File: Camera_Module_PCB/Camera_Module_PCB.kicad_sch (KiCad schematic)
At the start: 0 parts

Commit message: Added Multiple Component CAD Models
Added CAD models for the ESP32-S3, a USB C connector, a SD Card Slot, and an FPC Connector
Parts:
- added J1: FFC2A32-24-T, FFC2A32-24-T:GCT_FFC2A32-24-T, symbol 24 Pin FPC Connector:FFC2A32-24-T
- added J2: DM3AT-SF-PEJM5, DM3AT-SF-PEJM5:HRS_DM3AT-SF-PEJM5, symbol DM3AT-SF-PEJM5 SIM Card:DM3AT-SF-PEJM5
- added P1: USB_C_Plug_USB2.0, symbol Connector:USB_C_Plug_USB2.0
- added SW1: SW_Push, symbol Switch:SW_Push
- added U1: ESP32-S3, ESP32-S3:IC_ESP32-S3, symbol ESP32-S3:ESP32-S3
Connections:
- new net: P1.A1 (GND), P1.A12 (GND), P1.B1 (GND), P1.B12 (GND)
- new net: P1.A4 (VBUS), P1.A9 (VBUS), P1.B4 (VBUS), P1.B9 (VBUS)
- new net: J1.S1 (SHIELD), J1.S2 (SHIELD), J1.S3 (SHIELD), J1.S4 (SHIELD)
- new net VDD3P3: U1.2 (VDD3P3), U1.3 (VDD3P3)
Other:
- note added: "Not Sure if this is the type of USB C we want , but it seems like it"

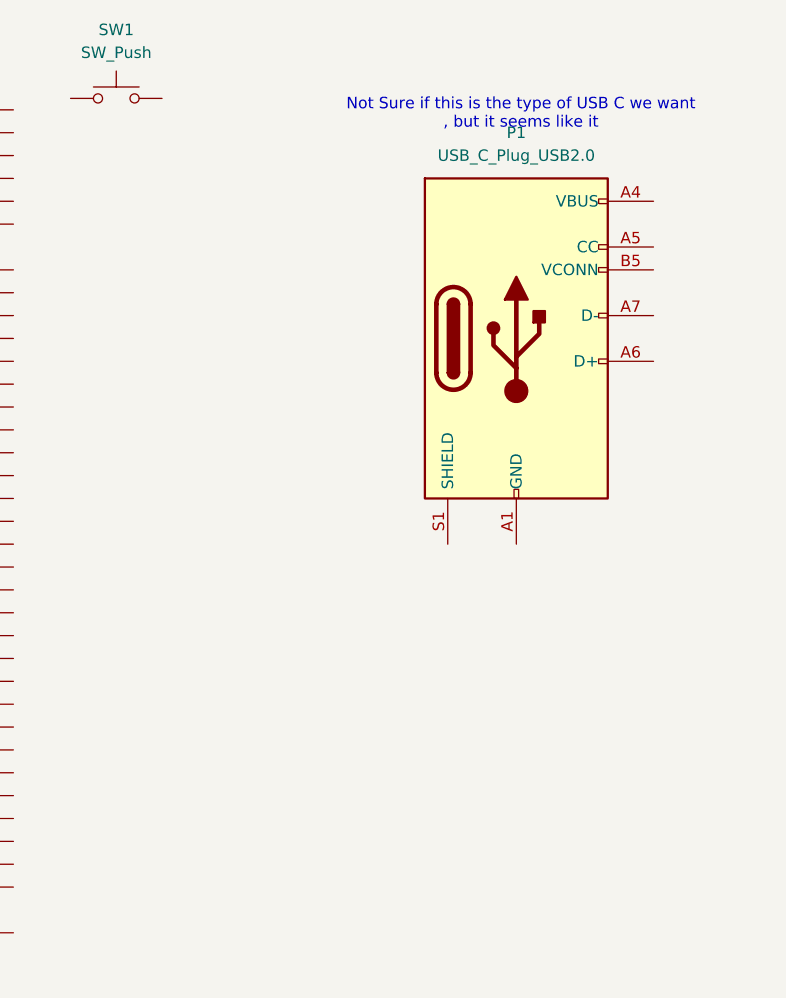
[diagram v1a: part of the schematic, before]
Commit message: Added Extra CAD Models for Voltage
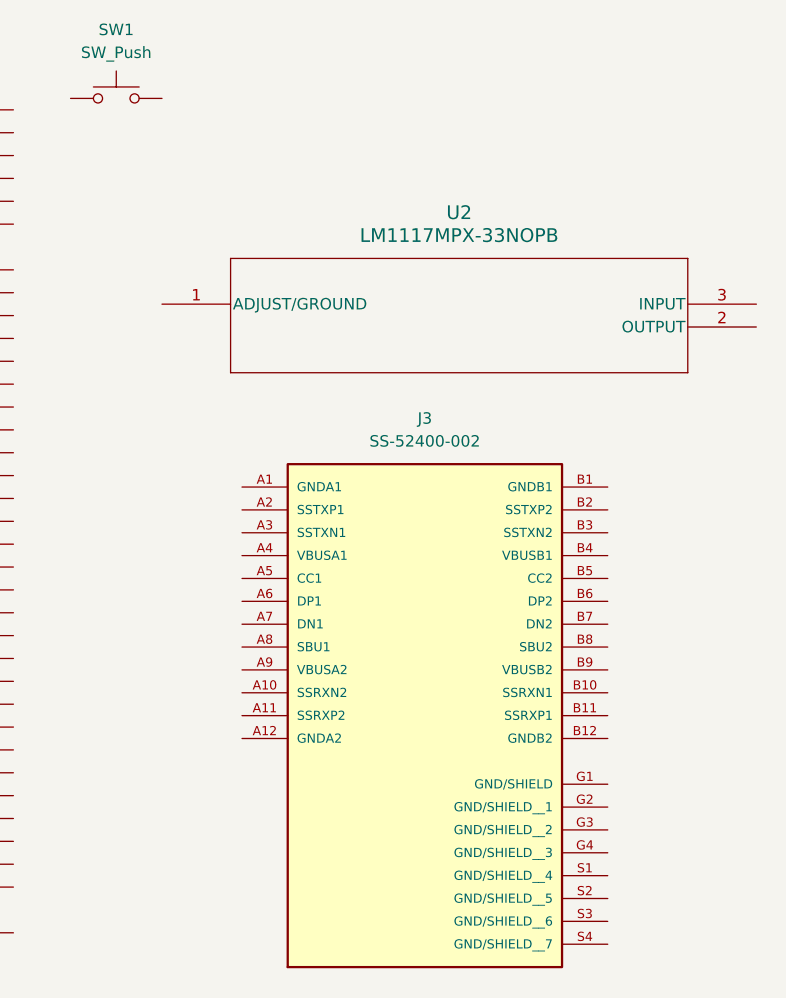
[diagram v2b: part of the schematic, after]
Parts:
- removed P1: USB_C_Plug_USB2.0, symbol Connector:USB_C_Plug_USB2.0
- added J3: SS-52400-002, SS-52400-002:BELFUSE_SS-52400-002, symbol SS-52400-002:SS-52400-002
- added U2: LM1117MPX-33NOPB, SOT223-318H_OSI, symbol LM117MPX-33NOPB:LM1117MPX-33NOPB
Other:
- note removed: "Not Sure if this is the type of USB C we want , but it seems like it"
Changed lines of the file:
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@@
 	(generator_version "9.0")
 	(paper "A4")
-	(text "Not Sure if this is the type of USB C we want\n, but it seems like it"
-		(exclude_from_sim no)
-		(at 220.218 24.638 0)
-		(effects
-			(font
-				(size 1.27 1.27)
-			)
-		)
-	)
 	(symbol
 		(lib_id "ESP32-S3:ESP32-S3")
@@
 	)
 	(symbol
-		(lib_id "Connector:USB_C_Plug_USB2.0")
-		(at 219.71 49.53 0)
+		(lib_id "LM117MPX-33NOPB:LM1117MPX-33NOPB")
+		(at 180.34 45.72 0)
 		(unit 1)
 		(exclude_from_sim no)
@@
 		(dnp no)
 		(fields_autoplaced yes)
-		(property "Reference" "P1"
-			(at 219.71 26.67 0)
-			(effects
-				(font
-					(size 1.27 1.27)
-				)
-			)
-		)
-		(property "Value" "USB_C_Plug_USB2.0"
-			(at 219.71 29.21 0)
-			(effects
-				(font
-					(size 1.27 1.27)
-				)
-			)
-		)
-		(property "Footprint" ""
-			(at 223.52 49.53 0)
-			(effects
-				(font
-					(size 1.27 1.27)
-				)
-				(hide yes)
-			)
-		)
-		(property "Datasheet" "https://www.usb.org/sites/default/files/documents/usb_type-c.zip"
-			(at 223.52 49.53 0)
-			(effects
-				(font
-					(size 1.27 1.27)
-				)
-				(hide yes)
-			)
-		)
-		(property "Description" "USB 2.0-only Type-C Plug connector"
-			(at 219.71 49.53 0)
-			(effects
-				(font
-					(size 1.27 1.27)
-				)
-				(hide yes)
-			)
-		)
-		(pin "B9"
-		)
-		(pin "A9"
-		)
-		(pin "S1"
-		)
-		(pin "B12"
-		)
-		(pin "B4"
-		)
-		(pin "A1"
-		)
-		(pin "A6"
-		)
-		(pin "B5"
-		)
-		(pin "A7"
-		)
-		(pin "A4"
-		)
-		(pin "A5"
-		)
-		(pin "B1"
-		)
-		(pin "A12"
+		(property "Reference" "U2"
+			(at 213.36 35.56 0)
+			(effects
+				(font
+					(size 1.524 1.524)
+				)
+			)
+		)
+		(property "Value" "LM1117MPX-33NOPB"
+			(at 213.36 38.1 0)
+			(effects
+				(font
+					(size 1.524 1.524)
+				)
+			)
+		)
+		(property "Footprint" "SOT223-318H_OSI"
+			(at 180.34 45.72 0)
+			(effects
+				(font
+					(size 1.27 1.27)
+					(italic yes)
+				)
+				(hide yes)
+			)
+		)
+		(property "Datasheet" "LM1117MPX-33NOPB"
+			(at 180.34 45.72 0)
+			(effects
+				(font
+					(size 1.27 1.27)
+					(italic yes)
+				)
+				(hide yes)
+			)
+		)
+		(property "Description" ""
+			(at 180.34 45.72 0)
+			(effects
+				(font
+					(size 1.27 1.27)
+				)
+				(hide yes)
+			)
+		)
+		(pin "3"
+		)
+		(pin "2"
+		)
+		(pin "1"
 		)
 		(instances
 			(project ""
 				(path "/e3d5a9d6-7dc8-43b3-bd64-189ae9cbab33"
-					(reference "P1")
+					(reference "U2")
+					(unit 1)
+				)
+			)
+		)
+	)
+	(symbol
+		(lib_id "SS-52400-002:SS-52400-002")
+		(at 209.55 81.28 0)
+		(unit 1)
+		(exclude_from_sim no)
+		(in_bom yes)
+		(on_board yes)
+		(dnp no)
+		(fields_autoplaced yes)
+		(property "Reference" "J3"
+			(at 209.55 58.42 0)
+			(effects
+				(font
+					(size 1.27 1.27)
+				)
+			)
+		)
+		(property "Value" "SS-52400-002"
+			(at 209.55 60.96 0)
+			(effects
+				(font
+					(size 1.27 1.27)
+				)
+			)
+		)
+		(property "Footprint" "SS-52400-002:BELFUSE_SS-52400-002"
+			(at 209.55 81.28 0)
+			(effects
+				(font
+					(size 1.27 1.27)
+				)
+				(justify bottom)
+				(hide yes)
+			)
+		)
+		(property "Datasheet" ""
+			(at 209.55 81.28 0)
+			(effects
+				(font
+					(size 1.27 1.27)
+				)
+				(hide yes)
+			)
+		)
+		(property "Description" ""
+			(at 209.55 81.28 0)
+			(effects
+				(font
+					(size 1.27 1.27)
+				)
+				(hide yes)
+			)
+		)
+		(property "PARTREV" "A0"
+			(at 209.55 81.28 0)
+			(effects
+				(font
+					(size 1.27 1.27)
+				)
+				(justify bottom)
+				(hide yes)
+			)
+		)
+		(property "STANDARD" "Manufacturer Recommendations"
+			(at 209.55 81.28 0)
+			(effects
+				(font
+					(size 1.27 1.27)
+				)
+				(justify bottom)
+				(hide yes)
+			)
+		)
+		(property "MAXIMUM_PACKAGE_HEIGHT" "2.96 mm"
+			(at 209.55 81.28 0)
+			(effects
+				(font
+					(size 1.27 1.27)
+				)
+				(justify bottom)
+				(hide yes)
+			)
+		)
+		(property "MANUFACTURER" "BelFuse"
+			(at 209.55 81.28 0)
+			(effects
+				(font
+					(size 1.27 1.27)
+				)
+				(justify bottom)
+				(hide yes)
+			)
+		)
+		(pin "B10"
+		)
+		(pin "B12"
+		)
+		(pin "G2"
+		)
+		(pin "A10"
+		)
+		(pin "B8"
+		)
+		(pin "A8"
+		)
+		(pin "S2"
+		)
+		(pin "A6"
+		)
+		(pin "A11"
+		)
+		(pin "A1"
+		)
+		(pin "A2"
+		)
+		(pin "A3"
+		)
+		(pin "A4"
+		)
+		(pin "A12"
+		)
+		(pin "B1"
+		)
+		(pin "B2"
+		)
+		(pin "B4"
+		)
+		(pin "A5"
+		)
+		(pin "A7"
+		)
+		(pin "B5"
+		)
+		(pin "A9"
+		)
+		(pin "B6"
+		)
+		(pin "B7"
+		)
+		(pin "B9"
+		)
+		(pin "B3"
+		)
+		(pin "B11"
+		)
+		(pin "G1"
+		)
+		(pin "G3"
+		)
+		(pin "G4"
+		)
+		(pin "S1"
+		)
+		(pin "S3"
+		)
+		(pin "S4"
+		)
+		(instances
+			(project ""
+				(path "/e3d5a9d6-7dc8-43b3-bd64-189ae9cbab33"
+					(reference "J3")
 					(unit 1)
 				)
@@
 	(sheet_instances
 		(path "/"
-			(page "1")
+			(page "2")
 		)
 	)

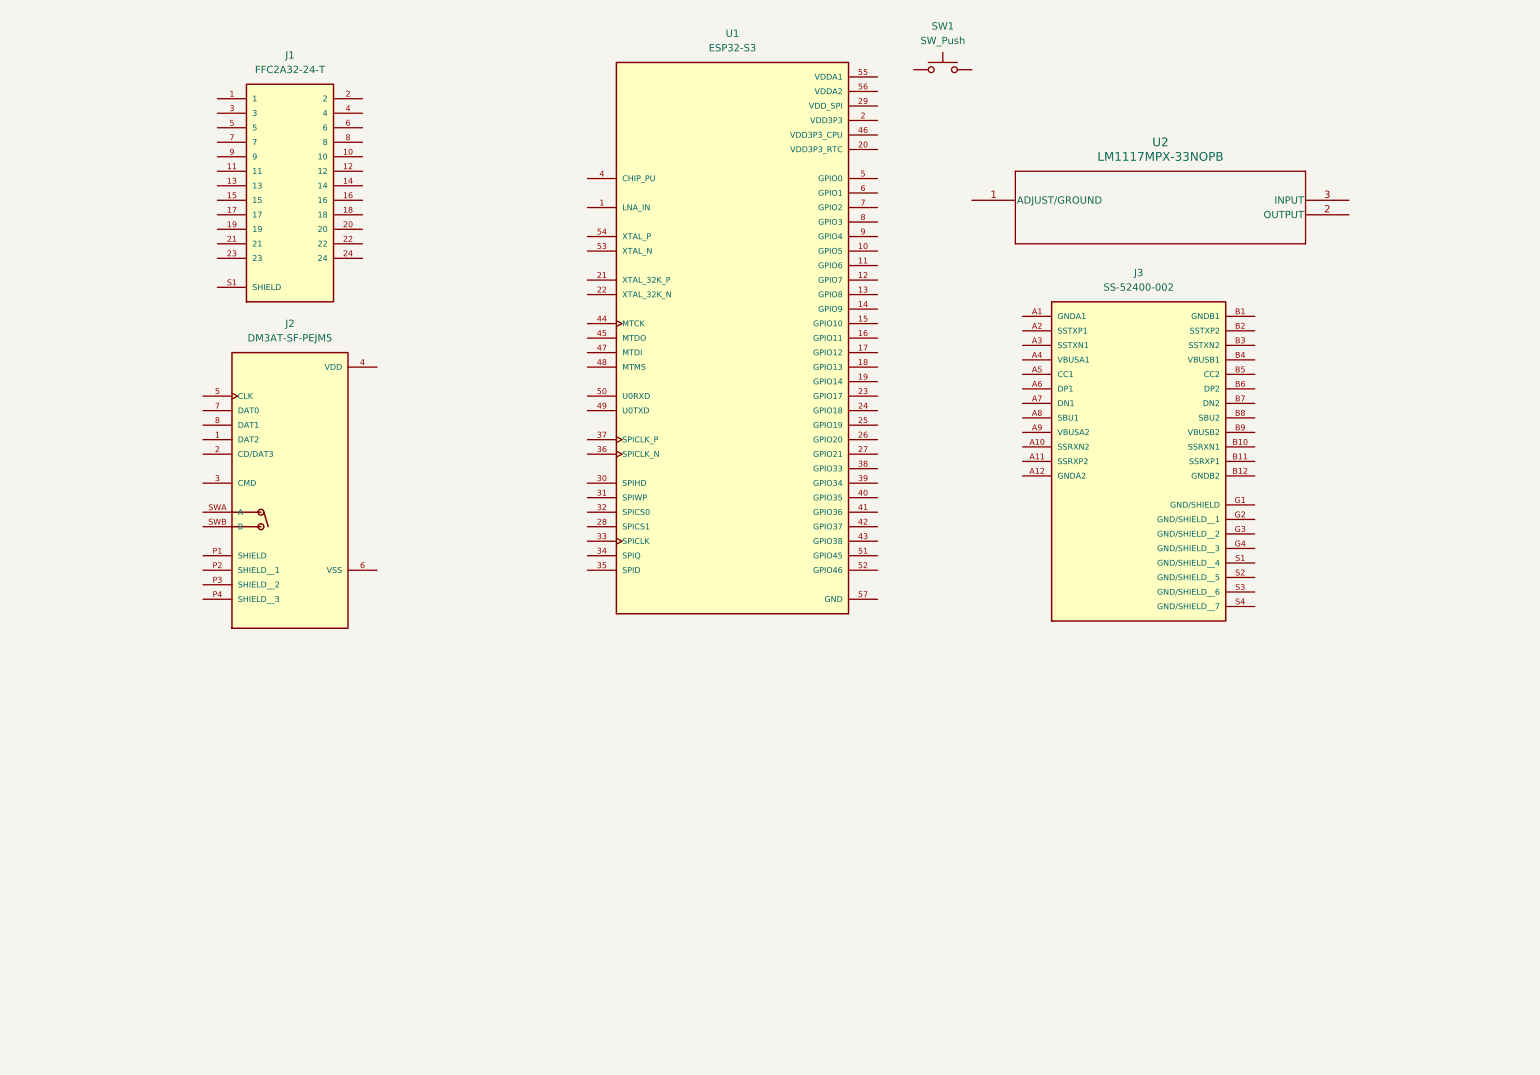
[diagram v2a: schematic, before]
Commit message: Moved Power Related Components to a new sheet
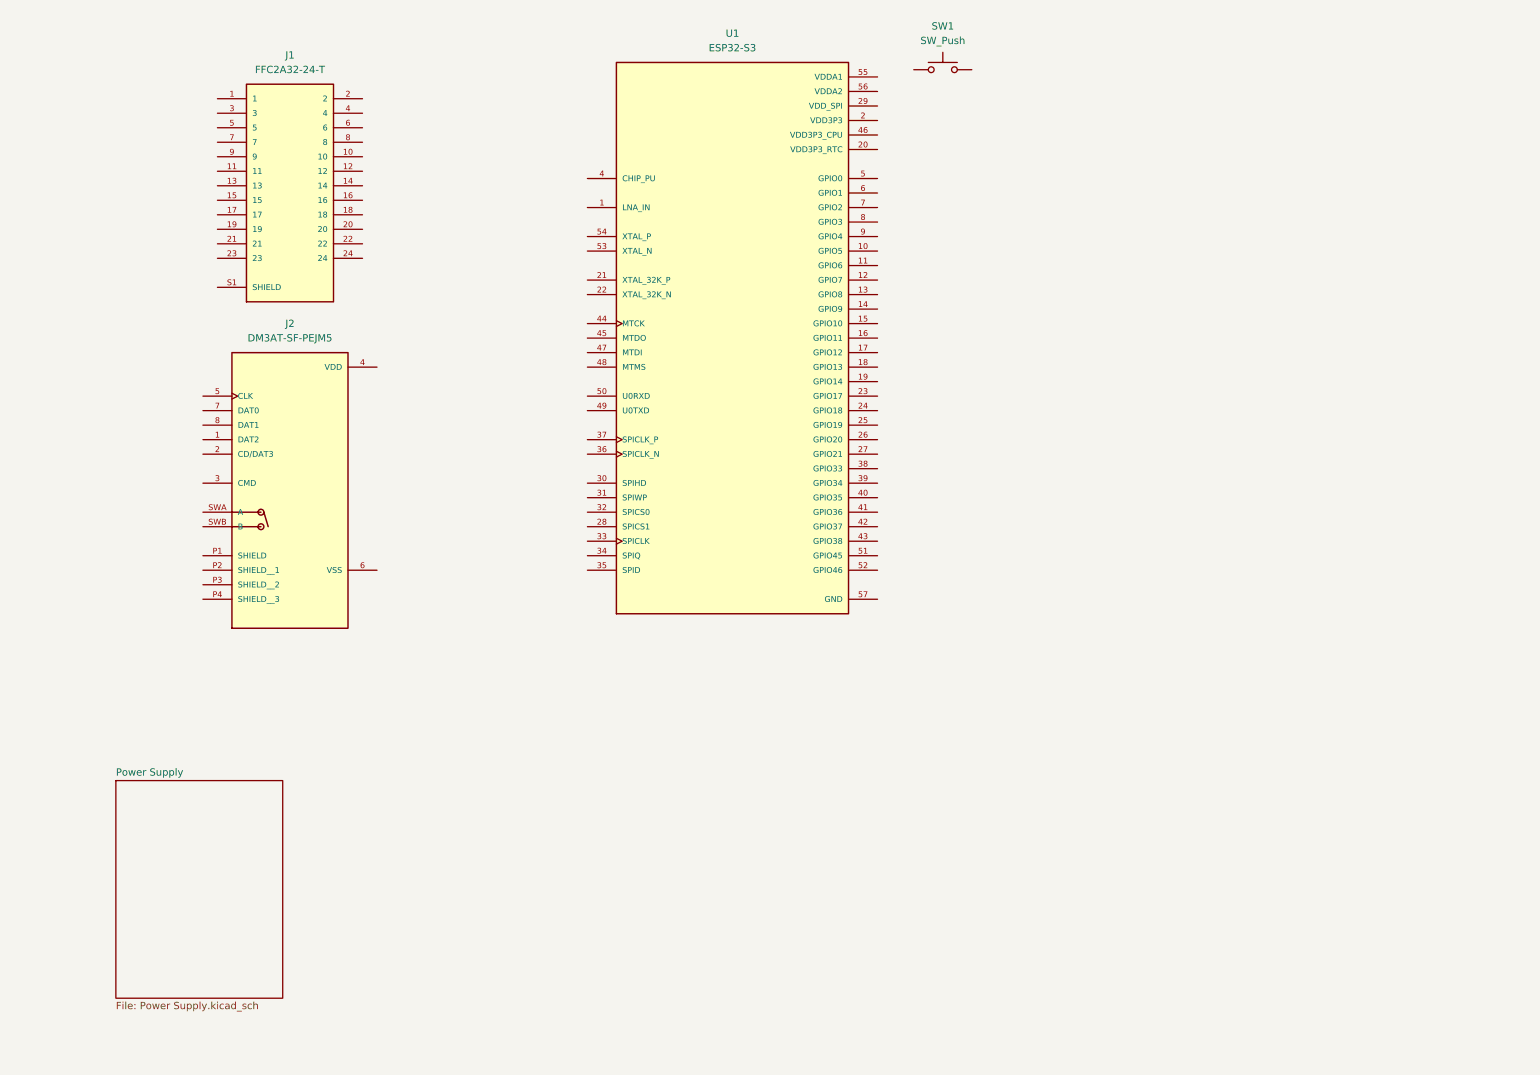
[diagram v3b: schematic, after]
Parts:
- removed J3: SS-52400-002, SS-52400-002:BELFUSE_SS-52400-002, symbol SS-52400-002:SS-52400-002
- removed U2: LM1117MPX-33NOPB, SOT223-318H_OSI, symbol LM117MPX-33NOPB:LM1117MPX-33NOPB
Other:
- added sheet Power Supply (Power Supply.kicad_sch)
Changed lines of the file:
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@@
-	)
-	(symbol
-		(lib_id "LM117MPX-33NOPB:LM1117MPX-33NOPB")
-		(at 180.34 45.72 0)
-		(unit 1)
-		(exclude_from_sim no)
-		(in_bom yes)
-		(on_board yes)
-		(dnp no)
-		(fields_autoplaced yes)
-		(property "Reference" "U2"
-			(at 213.36 35.56 0)
-			(effects
-				(font
-					(size 1.524 1.524)
-				)
-			)
-		)
-		(property "Value" "LM1117MPX-33NOPB"
-			(at 213.36 38.1 0)
-			(effects
-				(font
-					(size 1.524 1.524)
-				)
-			)
-		)
-		(property "Footprint" "SOT223-318H_OSI"
-			(at 180.34 45.72 0)
-			(effects
-				(font
-					(size 1.27 1.27)
-					(italic yes)
-				)
-				(hide yes)
-			)
-		)
-		(property "Datasheet" "LM1117MPX-33NOPB"
-			(at 180.34 45.72 0)
-			(effects
-				(font
-					(size 1.27 1.27)
-					(italic yes)
-				)
-				(hide yes)
-			)
-		)
-		(property "Description" ""
-			(at 180.34 45.72 0)
-			(effects
-				(font
-					(size 1.27 1.27)
-				)
-				(hide yes)
-			)
-		)
-		(pin "3"
-		)
-		(pin "2"
-		)
-		(pin "1"
-		)
-		(instances
-			(project ""
-				(path "/e3d5a9d6-7dc8-43b3-bd64-189ae9cbab33"
-					(reference "U2")
-					(unit 1)
-				)
-			)
-		)
-	)
-	(symbol
-		(lib_id "SS-52400-002:SS-52400-002")
-		(at 209.55 81.28 0)
-		(unit 1)
-		(exclude_from_sim no)
-		(in_bom yes)
-		(on_board yes)
-		(dnp no)
-		(fields_autoplaced yes)
-		(property "Reference" "J3"
-			(at 209.55 58.42 0)
-			(effects
-				(font
-					(size 1.27 1.27)
-				)
-			)
-		)
-		(property "Value" "SS-52400-002"
-			(at 209.55 60.96 0)
-			(effects
-				(font
-					(size 1.27 1.27)
-				)
-			)
-		)
-		(property "Footprint" "SS-52400-002:BELFUSE_SS-52400-002"
-			(at 209.55 81.28 0)
-			(effects
-				(font
-					(size 1.27 1.27)
-				)
-				(justify bottom)
-				(hide yes)
-			)
-		)
-		(property "Datasheet" ""
-			(at 209.55 81.28 0)
-			(effects
-				(font
-					(size 1.27 1.27)
-				)
-				(hide yes)
-			)
-		)
-		(property "Description" ""
-			(at 209.55 81.28 0)
-			(effects
-				(font
-					(size 1.27 1.27)
-				)
-				(hide yes)
-			)
-		)
-		(property "PARTREV" "A0"
-			(at 209.55 81.28 0)
-			(effects
-				(font
-					(size 1.27 1.27)
-				)
-				(justify bottom)
-				(hide yes)
-			)
-		)
-		(property "STANDARD" "Manufacturer Recommendations"
-			(at 209.55 81.28 0)
-			(effects
-				(font
-					(size 1.27 1.27)
-				)
-				(justify bottom)
-				(hide yes)
-			)
-		)
-		(property "MAXIMUM_PACKAGE_HEIGHT" "2.96 mm"
-			(at 209.55 81.28 0)
-			(effects
-				(font
-					(size 1.27 1.27)
-				)
-				(justify bottom)
-				(hide yes)
-			)
-		)
-		(property "MANUFACTURER" "BelFuse"
-			(at 209.55 81.28 0)
-			(effects
-				(font
-					(size 1.27 1.27)
-				)
-				(justify bottom)
-				(hide yes)
-			)
-		)
-		(pin "B10"
-		)
-		(pin "B12"
-		)
-		(pin "G2"
-		)
-		(pin "A10"
-		)
-		(pin "B8"
-		)
-		(pin "A8"
-		)
-		(pin "S2"
-		)
-		(pin "A6"
-		)
-		(pin "A11"
-		)
-		(pin "A1"
-		)
-		(pin "A2"
-		)
-		(pin "A3"
-		)
-		(pin "A4"
-		)
-		(pin "A12"
-		)
-		(pin "B1"
-		)
-		(pin "B2"
-		)
-		(pin "B4"
-		)
-		(pin "A5"
-		)
-		(pin "A7"
-		)
-		(pin "B5"
-		)
-		(pin "A9"
-		)
-		(pin "B6"
-		)
-		(pin "B7"
-		)
-		(pin "B9"
-		)
-		(pin "B3"
-		)
-		(pin "B11"
-		)
-		(pin "G1"
-		)
-		(pin "G3"
-		)
-		(pin "G4"
-		)
-		(pin "S1"
-		)
-		(pin "S3"
-		)
-		(pin "S4"
-		)
-		(instances
-			(project ""
-				(path "/e3d5a9d6-7dc8-43b3-bd64-189ae9cbab33"
-					(reference "J3")
-					(unit 1)
-				)
-			)
-		)
 	)
 	(symbol
@@
 				)
 			)
+		)
+	)
+	(sheet
+		(at 30.48 147.32)
+		(size 29.21 38.1)
+		(exclude_from_sim no)
+		(in_bom yes)
+		(on_board yes)
+		(dnp no)
+		(fields_autoplaced yes)
+		(stroke
+			(width 0.1524)
+			(type solid)
+		)
+		(fill
+			(color 0 0 0 0.0000)
+		)
+		(property "Sheetname" "Power Supply"
+			(at 30.48 146.6084 0)
+			(effects
+				(font
+					(size 1.27 1.27)
+				)
+				(justify left bottom)
+			)
+		)
+		(property "Sheetfile" "Power Supply.kicad_sch"
+			(at 30.48 186.0046 0)
+			(effects
+				(font
+					(size 1.27 1.27)
+				)
+				(justify left top)
+			)
+		)
+		(instances
+			(project "Camera_Module_PCB"
+				(path "/e3d5a9d6-7dc8-43b3-bd64-189ae9cbab33"
+					(page "2")
+				)
+			)
